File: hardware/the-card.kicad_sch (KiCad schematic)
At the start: 53 parts, among them J1 TYPE-C-31-M-12, J2 FPC 0.5-24P LTH2.0, Q1 SI2301CDS-T1-GE3, Q2 SI2301CDS-T1-GE3, SW1 TS-1187A-B-A-B, SW2 TS-1187A-B-A-B, SW3 TS-1187A-B-A-B, SW4 TS-1187A-B-A-B, U1 ESP32-S3-WROOM-1-N8R2, U10 USBLC6-2SC6, U2 ST25DV04KC-IE8S3, U3 LSM6DSOTR, U4 SHT40-BD1B-R2, U5 MAX17048G+T10, U6 TP4056_C382139, U7 DW01A_C18164398, U8 FS8205A, U9 ME6211C33M5G-N

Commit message: feat(hardware): prepare schematic for pcb layout
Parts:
- removed C_bat, C_imu2, C_mcu2, C_vbus: 10uF, Capacitor_SMD:C_0603_1608Metric, symbol passives:CL10A106KP8NNNC
- removed C_btn1, C_btn2, C_btn3, C_btn4, C_dprot, C_fg, C_imu1, C_led, C_mcu1, C_nfc, C_sht, C_vb: 100nF, Capacitor_SMD:C_0402_1005Metric, symbol passives:CL05B104KO5NNNC
- removed C_en, C_epdvdd, C_ldoi, C_ldoo: 1uF, Capacitor_SMD:C_0603_1608Metric, symbol passives:CL10A106KP8NNNC
- removed R_cc1, R_cc2: 5.1k, Resistor_SMD:R_0402_1005Metric, symbol passives:0402WGF1002TCE
- removed R_chrg, R_en, R_io0, R_q1g, R_q2g: 10k, Resistor_SMD:R_0402_1005Metric, symbol passives:0402WGF1002TCE
- removed R_dvcc: 470, Resistor_SMD:R_0402_1005Metric, symbol passives:0402WGF1002TCE
- removed R_dvm: 2k, Resistor_SMD:R_0402_1005Metric, symbol passives:0402WGF1002TCE
- removed R_prog: 1.2k, Resistor_SMD:R_0402_1005Metric, symbol passives:0402WGF1002TCE
- removed R_scl, R_sda: 4.7k, Resistor_SMD:R_0402_1005Metric, symbol passives:0402WGF1002TCE
- removed R_vbh: 1M, Resistor_SMD:R_0402_1005Metric, symbol passives:0402WGF1002TCE
- removed R_vbl: 300k, Resistor_SMD:R_0402_1005Metric, symbol passives:0402WGF1002TCE
- added C1, C10, C11, C12, C14, C15, C16, C17, C18, C19, C4, C7: 100nF, Capacitor_SMD:C_0402_1005Metric, symbol passives:CL05B104KO5NNNC
- added C13, C2, C5, C6: 10uF, Capacitor_SMD:C_0603_1608Metric, symbol passives:CL10A106KP8NNNC
- added C20, C21: 4.7uF 25V, Capacitor_SMD:C_0805_2012Metric, symbol passives:CL10A106KP8NNNC
- added C22, C23, C24, C25, C26, C27, C28: 1uF 25V, Capacitor_SMD:C_0805_2012Metric, symbol passives:CL10A106KP8NNNC
- added C3, C8, C9: 1uF, Capacitor_SMD:C_0603_1608Metric, symbol passives:CL10A106KP8NNNC
- added D2, D3, D4: MBR0530, Diode_SMD:D_SOD-123, symbol Device:D
- added J3: BATTERY 1S JST-PH, Connector_JST:JST_PH_S2B-PH-K_1x02_P2.00mm_Horizontal, symbol Connector_Generic:Conn_01x02
- added L1: SRU5016-470Y 47uH, Inductor_SMD:L_Bourns_SRU5016_5.2x5.2mm, symbol Device:L
- added Q3: Si1304BDL, Package_TO_SOT_SMD:SOT-323_SC-70, symbol Transistor_FET:Q_NMOS_GSD
- added R1, R11, R12, R2, R8: 10k, Resistor_SMD:R_0402_1005Metric, symbol passives:0402WGF1002TCE
- added R10: 2k, Resistor_SMD:R_0402_1005Metric, symbol passives:0402WGF1002TCE
- added R13, R14: 4.7k, Resistor_SMD:R_0402_1005Metric, symbol passives:0402WGF1002TCE
- added R15, R3: 1M, Resistor_SMD:R_0402_1005Metric, symbol passives:0402WGF1002TCE
- added R16: 2.2, Resistor_SMD:R_0402_1005Metric, symbol passives:0402WGF1002TCE
- added R4: 300k, Resistor_SMD:R_0402_1005Metric, symbol passives:0402WGF1002TCE
- added R5, R6: 5.1k, Resistor_SMD:R_0402_1005Metric, symbol passives:0402WGF1002TCE
- added R7: 2.2k, Resistor_SMD:R_0402_1005Metric, symbol passives:0402WGF1002TCE
- added R9: 470, Resistor_SMD:R_0402_1005Metric, symbol passives:0402WGF1002TCE
- added TP1: +BAT, TestPoint:TestPoint_Pad_D1.0mm, symbol Connector:TestPoint
- added TP2: BAT_NEG, TestPoint:TestPoint_Pad_D1.0mm, symbol Connector:TestPoint
- added TP3: +3V3, TestPoint:TestPoint_Pad_D1.0mm, symbol Connector:TestPoint
- added TP4: GND, TestPoint:TestPoint_Pad_D1.0mm, symbol Connector:TestPoint
- added TP5: EN, TestPoint:TestPoint_Pad_D1.0mm, symbol Connector:TestPoint
- added TP6: IO0, TestPoint:TestPoint_Pad_D1.0mm, symbol Connector:TestPoint
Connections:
- net NFC_ANT_B is gone; now on net NFC_ANTENNA: U2.3 (AC1)
- net +3V3: now also U3.12 (CS), U3.5 (VDDIO), U3.8 (VDD), U4.3 (VDD), C1.1, C11.1, C12.1, C13.1, C14.1, C2.1, C9.1, R1.1, R11.1, R12.1, R13.1, R14.1, R2.1, R8.1, TP3.1
- net +BAT: now also C10.1, C6.1, C8.1, J3.1 (Pin_1), R3.1, R9.1, TP1.1
- net AUX_3V3: now also C15.1; no longer U3.12 (CS), U3.5 (VDDIO), U3.8 (VDD), U4.3 (VDD)
- net BTN_DOWN: now also C17.1
- net BTN_MENU: now also C19.1
- net BTN_SEL: now also C18.1
- net BTN_UP: now also C16.1
- net EPD_GDR: now also Q3.1 (G), R15.1
- net EPD_PWR_EN: now also R12.2
- net EPD_RESE: now also Q3.2 (S), R16.1
- net EPD_VCOM: now also C28.1
- net EPD_VGH: now also C25.1, D4.1 (K)
- net EPD_VGL: now also C27.1, D2.2 (A)
- net EPD_VSH1: now also C24.1
- net EPD_VSH2: now also C23.1
- net EPD_VSL: now also C26.1
- net GND: now also C1.2, C10.2, C11.2, C12.2, C13.2, C14.2, C15.2, C16.2, C17.2, C18.2, C19.2, C2.2, C20.2, C22.2, C23.2, C24.2, C25.2, C26.2, C27.2, C28.2, C3.2, C4.2, C5.2, C6.2, C8.2, C9.2, D3.1 (K), R10.1, R15.2, R16.2, R4.2, R5.2, R6.2, R7.2, TP4.1; no longer U4.5 (EP)
- net I2C_SCL: now also R13.2
- net I2C_SDA: now also R14.2
- net PWR_AUX: now also R11.2
- net VBUS: now also C5.1
- net ~CHRG: now also R8.2
- net at U1.39 (IO1): now also C4.1, R3.2, R4.1
- net MCU_EN: now reaches U1.3 (EN)
- net MCU_EN: now also C3.1, R1.2, TP5.1
- net at U7.3 (COUT), U7.6 (VSS), U8.2 (S1)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: now also C7.2, J3.2 (Pin_2), TP2.1; no longer U7.1 (DOUT), U7.5 (VDD), U8.5 (G2)
- net EPD_VDD_CORE: now reaches J2.18
- net EPD_VDD_CORE: now also C22.1
- net at U7.2 (VM): now also R10.2
- net MCU_BOOT: now reaches U1.27 (IO0)
- net MCU_BOOT: now also R2.2, TP6.1
- net at U6.2 (PROG): now also R7.1
- net at J1.B5 (CC2): now also R6.1
- net at J1.A5 (CC1): now also R5.1
- net EPD_NC1: no longer names the net of J2.1
- net EPD_NC4: no longer names the net of J2.4
- net EPD_TSCL: no longer names the net of J2.6
- net EPD_TSDA: no longer names the net of J2.7
- net EPD_VDD renamed EPD_VCI
- net EPD_VCI: now also C20.1, L1.1
- net EPD_VPP: no longer names the net of J2.19
- net MOTOR_PWM: no longer names the net of U1.23 (IO21)
- net NFC_ANT_A renamed NFC_ANTENNA
- net NFC_EH: no longer names the net of U2.1 (V_EH)
- new net: C21.1, D2.1 (K), D3.2 (A)
- new net: C7.1, R9.2, U7.5 (VDD)
- new net: C21.2, D4.2 (A), L1.2, Q3.3 (D)
- new net: U7.1 (DOUT), U8.5 (G2)
- no-connect marks 33 -> 41
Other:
- note added: "Panel-specific SSD1680 booster and 25 V rail capacitors"
- note removed: "Panel booster and high-voltage pins remain named for PCB review."
- moved on the sheet: J2

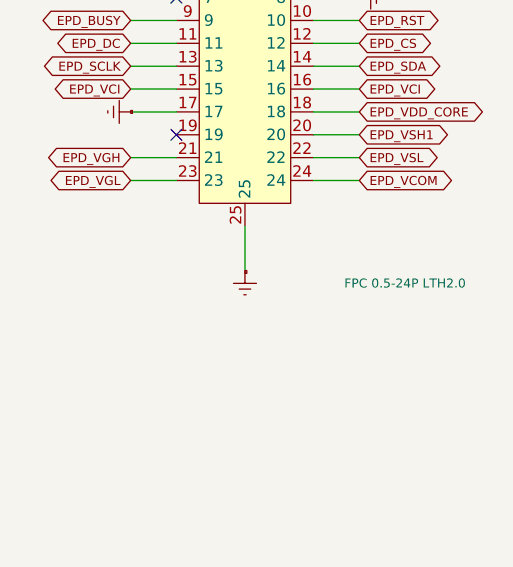
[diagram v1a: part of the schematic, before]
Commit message: fix(hardware): correct display FPC connector
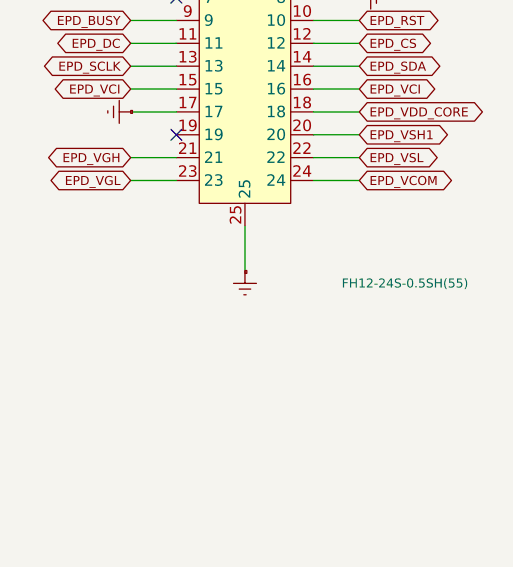
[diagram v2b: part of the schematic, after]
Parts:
- J2: value FPC 0.5-24P LTH2.0 -> FH12-24S-0.5SH(55); footprint the-card:FPC-SMD_FPC-0.5-24P-LTH2.0 -> the-card:Hirose_FH12-24S-0.5SH_1x24-2MP_P0.50mm_Horizontal
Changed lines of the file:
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@@
 			(effects (font (size 1.2 1.2) (bold yes)))
 		)
-		(property "Value" "FPC 0.5-24P LTH2.0"
+		(property "Value" "FH12-24S-0.5SH(55)"
 			(at 576.58 323.85 0)
 			(effects (font (size 1 1)))
 		)
-		(property "Footprint" "the-card:FPC-SMD_FPC-0.5-24P-LTH2.0"
+		(property "Footprint" "the-card:Hirose_FH12-24S-0.5SH_1x24-2MP_P0.50mm_Horizontal"
 			(at 558.8 298.45 0)
 			(effects (font (size 1 1)) (hide yes))
 		)
-		(property "Datasheet" "https://www.lcsc.com/datasheet/C6081230.pdf"
+		(property "Datasheet" "https://www.hirose.com/product/p/CL0586-0521-0-55"
 			(at 558.8 298.45 0)
 			(effects (font (size 1 1)) (hide yes))

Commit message: fix(hardware): harden design for fabrication
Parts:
- R10: value 2k -> 1k
- R9: value 470 -> 100
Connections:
- net at C7.2, J3.2 (Pin_2), TP2.1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: now also U7.1 (DOUT); no longer U7.3 (COUT)
- net at U8.5 (G2): now also U7.3 (COUT); no longer U7.1 (DOUT)
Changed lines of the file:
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@@
 			(effects (font (size 1.2 1.2) (bold yes)))
 		)
-		(property "Value" "470"
+		(property "Value" "100"
 			(at 60.96 153.67 0)
 			(effects (font (size 1 1)))
@@
 			(effects (font (size 1.2 1.2) (bold yes)))
 		)
-		(property "Value" "2k"
+		(property "Value" "1k"
 			(at 120.65 167.64 0)
 			(effects (font (size 1 1)))
@@
 	)
 	(wire
-		(pts (xy 105.41 162.56) (xy 143.51 162.56))
-		(stroke (width 0) (type default))
-	)
-	(wire
-		(pts (xy 143.51 162.56) (xy 143.51 168.91))
-		(stroke (width 0) (type default))
-	)
-	(wire
-		(pts (xy 105.41 167.64) (xy 161.29 167.64))
-		(stroke (width 0) (type default))
-	)
-	(wire
-		(pts (xy 161.29 167.64) (xy 161.29 168.91))
-		(stroke (width 0) (type default))
-	)
+		(pts (xy 105.41 167.64) (xy 143.51 167.64))
+		(stroke (width 0) (type default))
+	)
+	(wire
+		(pts (xy 143.51 167.64) (xy 143.51 168.91))
+		(stroke (width 0) (type default))
+	)
+	(wire
+		(pts (xy 105.41 162.56) (xy 161.29 162.56))
+		(stroke (width 0) (type default))
+	)
+	(wire
+		(pts (xy 161.29 162.56) (xy 161.29 168.91))
+		(stroke (width 0) (type default))
+	)

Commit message: feat(hardware): add fabrication release workflow
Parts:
- TP1, TP2, TP3, TP4, TP5, TP6: now left out of the parts list
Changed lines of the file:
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@@
 		(unit 1)
 		(exclude_from_sim no)
-		(in_bom yes)
+		(in_bom no)
 		(on_board yes)
 		(dnp no)
@@
 		(unit 1)
 		(exclude_from_sim no)
-		(in_bom yes)
+		(in_bom no)
 		(on_board yes)
 		(dnp no)
@@
 		(unit 1)
 		(exclude_from_sim no)
-		(in_bom yes)
+		(in_bom no)
 		(on_board yes)
 		(dnp no)
@@
 		(unit 1)
 		(exclude_from_sim no)
-		(in_bom yes)
+		(in_bom no)
 		(on_board yes)
 		(dnp no)
@@
 		(unit 1)
 		(exclude_from_sim no)
-		(in_bom yes)
+		(in_bom no)
 		(on_board yes)
 		(dnp no)
@@
 		(unit 1)
 		(exclude_from_sim no)
-		(in_bom yes)
-		(on_board yes)
-		(dnp no)
+		(in_bom no)
+		(on_board yes)
+		(dnp no)

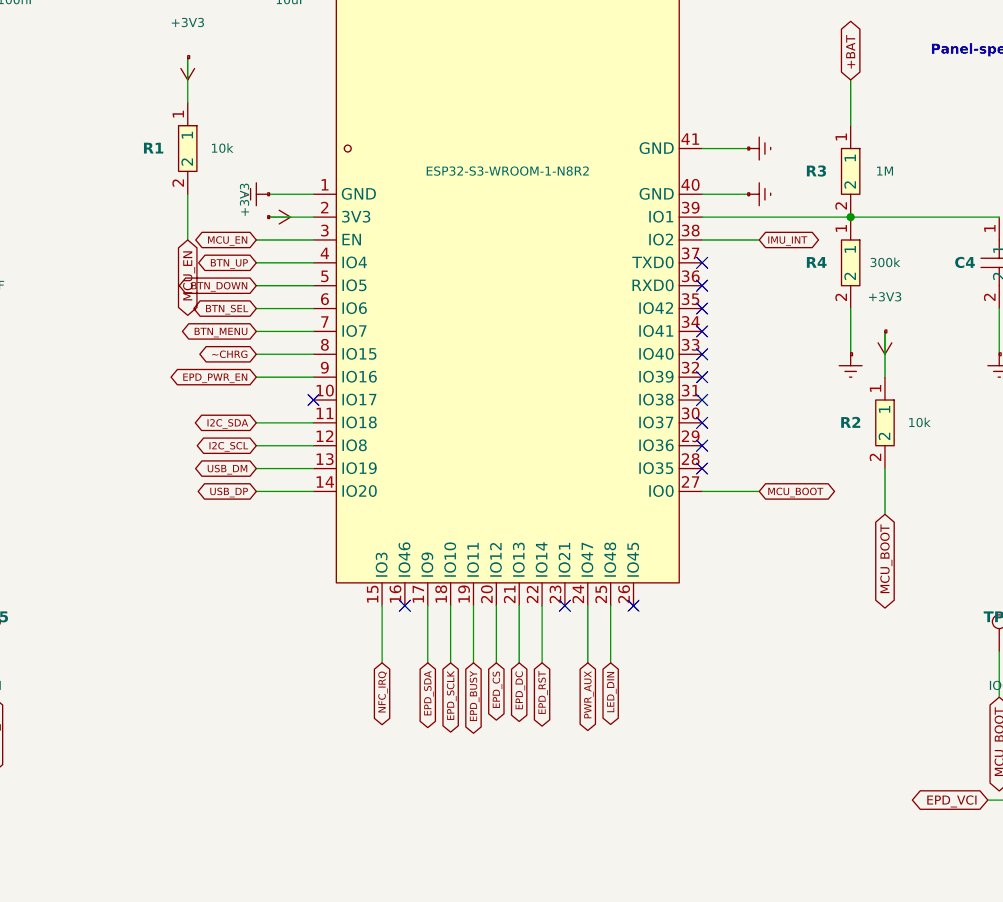
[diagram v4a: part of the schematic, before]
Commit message: feat(hardware): upgrade MCU memory variant
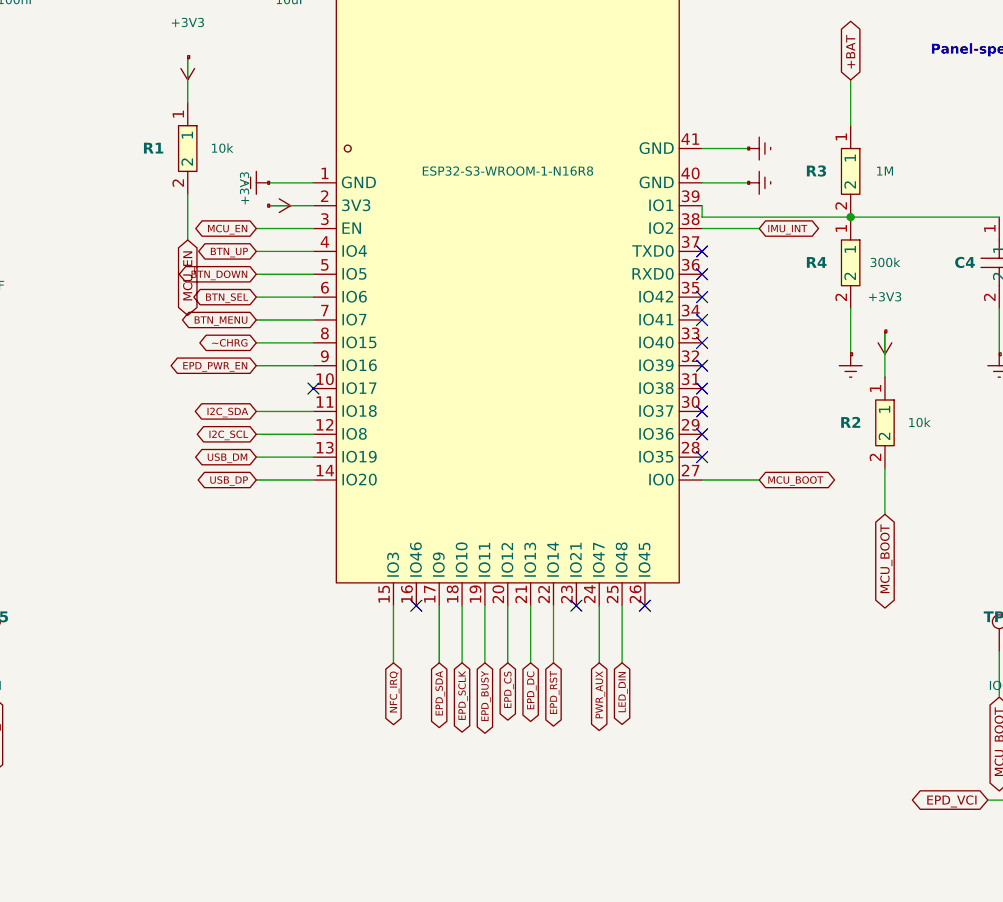
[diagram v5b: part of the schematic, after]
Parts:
- U1: value ESP32-S3-WROOM-1-N8R2 -> ESP32-S3-WROOM-1-N16R8

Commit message: fix(hardware): source SMT battery connector and inductor
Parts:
- J3: value BATTERY 1S JST-PH -> S2B-PH-SM4-TB(LF)(SN); footprint Connector_JST:JST_PH_S2B-PH-K_1x02_P2.00mm_Horizontal -> Connector_JST:JST_PH_S2B-PH-SM4-TB_1x02-1MP_P2.00mm_Horizontal
- L1: value SRU5016-470Y 47uH -> XRNR5020-47uH/M 47uH; footprint Inductor_SMD:L_Bourns_SRU5016_5.2x5.2mm -> the-card:IND-SMD_L5.0-W5.0_XRNR5020
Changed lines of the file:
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@@
 			(effects (font (size 1.2 1.2) (bold yes)))
 		)
-		(property "Value" "BATTERY 1S JST-PH"
+		(property "Value" "S2B-PH-SM4-TB(LF)(SN)"
 			(at 25.4 182.88 0)
 			(effects (font (size 1 1)))
 		)
-		(property "Footprint" "Connector_JST:JST_PH_S2B-PH-K_1x02_P2.00mm_Horizontal"
+		(property "Footprint" "Connector_JST:JST_PH_S2B-PH-SM4-TB_1x02-1MP_P2.00mm_Horizontal"
 			(at 25.4 177.8 0)
 			(effects (font (size 1 1)) (hide yes))
@@
 			(effects (font (size 1.2 1.2) (bold yes)))
 		)
-		(property "Value" "SRU5016-470Y 47uH"
+		(property "Value" "XRNR5020-47uH/M 47uH"
 			(at 400.05 287.02 0)
 			(effects (font (size 1 1)))
 		)
-		(property "Footprint" "Inductor_SMD:L_Bourns_SRU5016_5.2x5.2mm"
+		(property "Footprint" "the-card:IND-SMD_L5.0-W5.0_XRNR5020"
 			(at 400.05 279.4 0)
 			(effects (font (size 1 1)) (hide yes))
